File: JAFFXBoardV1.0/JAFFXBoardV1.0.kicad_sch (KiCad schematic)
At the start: 21 parts, among them J1 1/4inLineIn, J2 1/4inLineOut, SW1 DPDT_Slide_SMD_7.2x3.5mm, SW1 SW_SPST, SW2 SW_SPST, SW3 SW_SPST, SW4 SW_SPST, SW5 SW_SPST, SW6 SW_SPST, SW7 SW_SPDT, U1 LM358

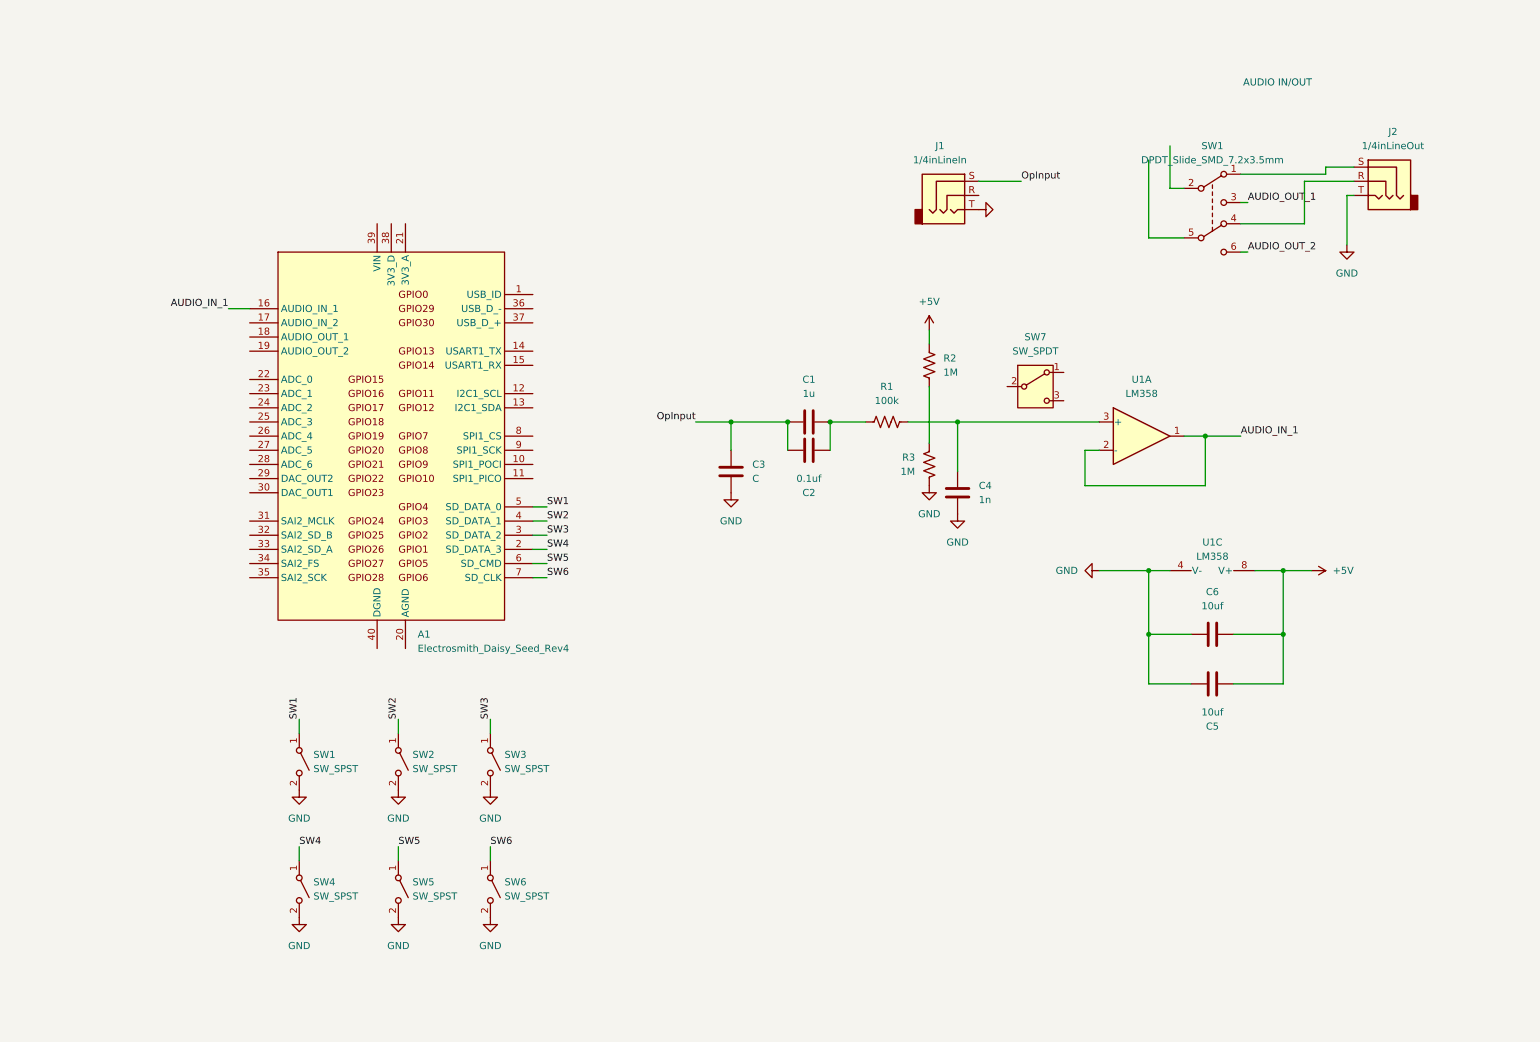
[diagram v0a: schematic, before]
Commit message: added argb and all op amps, still need to clean it up and figure switch situation
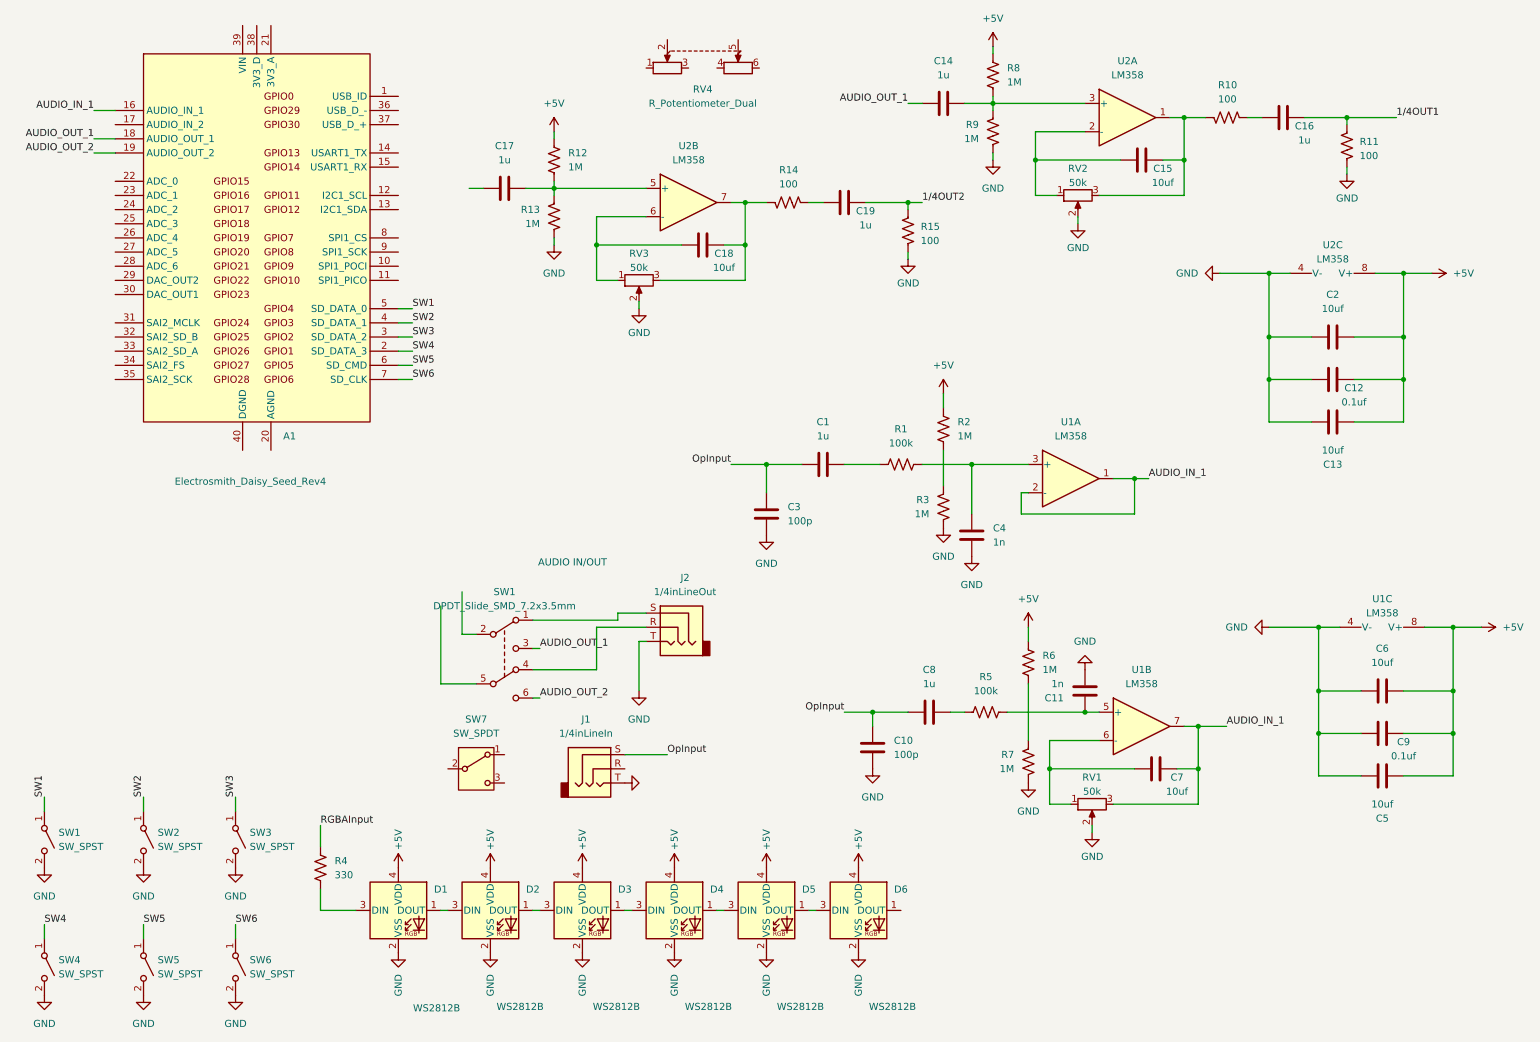
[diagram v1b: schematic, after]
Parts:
- added C10: 100p, symbol Device:C
- added C11: 1n, symbol Device:C
- added C12, C9: 0.1uf, symbol Device:C
- added C13, C15, C18, C7: 10uf, symbol Device:C
- added C14, C16, C17, C19, C8: 1u, symbol Device:C
- added D1, D2, D3, D4, D5, D6: WS2812B, SparkFun-LED:WS2812_2020, symbol SparkFun-LED:WS2812B_2020
- added R10, R11, R14, R15: 100, symbol Device:R_US
- added R12, R13, R6, R7, R8, R9: 1M, symbol Device:R_US
- added R4: 330, symbol Device:R_US
- added R5: 100k, symbol Device:R_US
- added RV1, RV2, RV3: 50k, symbol Device:R_Potentiometer
- added RV4: R_Potentiometer_Dual, symbol Device:R_Potentiometer_Dual
- added unit 2 of U1
- added U2: LM358, symbol Amplifier_Operational:LM358
- C2: value 0.1uf -> 10uf
- C3: value C -> 100p
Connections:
- net +5V: now also C2.2, C12.1, C13.2, C9.1, D1.4 (VDD), D2.4 (VDD), D3.4 (VDD), D4.4 (VDD), D5.4 (VDD), D6.4 (VDD), R12.2, R6.2, R8.2, U2.8 (V+)
- net AUDIO_IN_1: now also C7.1, RV1.3, U1.7
- net AUDIO_OUT_1: now also A1.18 (AUDIO_OUT_1), C14.1
- net AUDIO_OUT_2: now also A1.19 (AUDIO_OUT_2)
- net GND: now also C2.1, C10.1, C11.1, C12.2, C13.1, C9.2, D1.2 (VSS), D2.2 (VSS), D3.2 (VSS), D4.2 (VSS), D5.2 (VSS), D6.2 (VSS), R11.2, R13.1, R15.2, R7.1, R9.1, RV1.2, RV2.2, RV3.2, U2.4 (V-)
- net OpInput: now also C10.2, C8.1; no longer C2.2
- net at C1.2, R1.1: no longer C2.1
- new net: C19.2, R14.2
- new net: C15.1, R10.1, RV2.3, U2.1
- new net: C15.2, RV2.1, U2.2 (-)
- new net: R6.1, R7.2
- new net: C11.2, R5.2, U1.5 (+)
- new net: C7.2, RV1.1, U1.6 (-)
- new net: C18.1, R14.1, RV3.3, U2.7
- new net: D1.3 (DIN), R4.1
- new net: D1.1 (DOUT), D2.3 (DIN)
- new net: C17.2, R12.1, R13.2, U2.5 (+)
- new net: C18.2, RV3.1, U2.6 (-)
- new net: C16.2, R10.2
- new net: C14.2, R8.1, R9.2, U2.3 (+)
- new net: D5.1 (DOUT), D6.3 (DIN)
- new net: D4.1 (DOUT), D5.3 (DIN)
- new net: D3.1 (DOUT), D4.3 (DIN)
- new net: D2.1 (DOUT), D3.3 (DIN)
- new net: C8.2, R5.1
- new net 1/4OUT1: C16.1, R11.1
- new net 1/4OUT2: C19.1, R15.1
- new net RGBAInput: R4.2
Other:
- moved on the sheet: A1, C1, C3, C4, C5, C6, J1, J2, R1, R2, R3, SW1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
